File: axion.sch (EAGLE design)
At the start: 146 parts, among them IC1 3.3V, IC2 5V, Q2 12.288Mhz, U10 MIC2039, U11 WM8731, U2 Intel Edison, U4 FT232RLSSOP, U5 PCA9306D, U6 74HC4050, U7 TPA2005D1DGN, X1 MKDSN1,5/2-5,08, X2 ZX62R-AB-5P, X3 ST-005-G, X4 ZX62R-B-5P

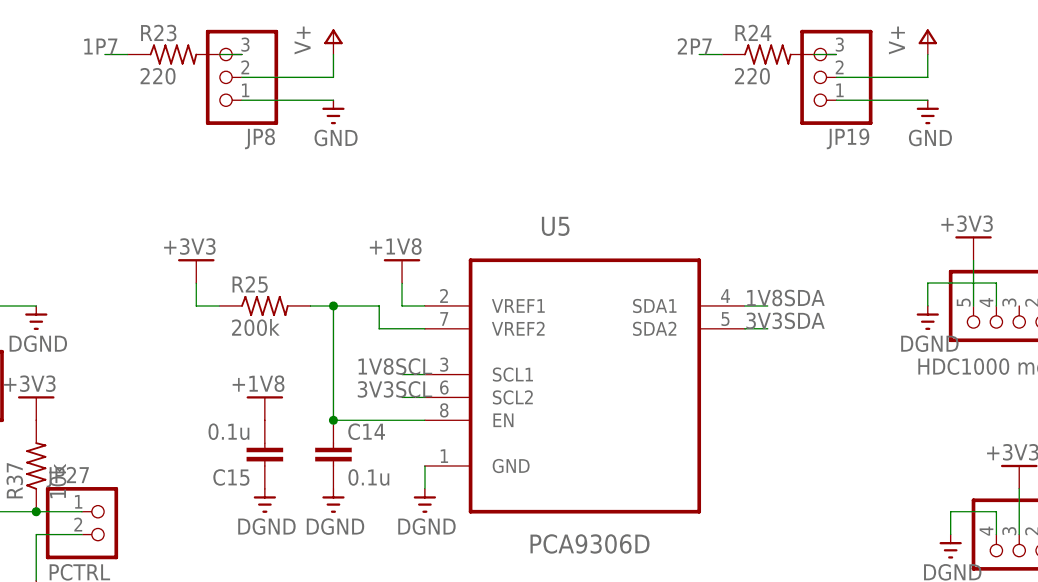
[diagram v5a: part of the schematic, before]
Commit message: Add 820 pullup to 1v8 side of I2c
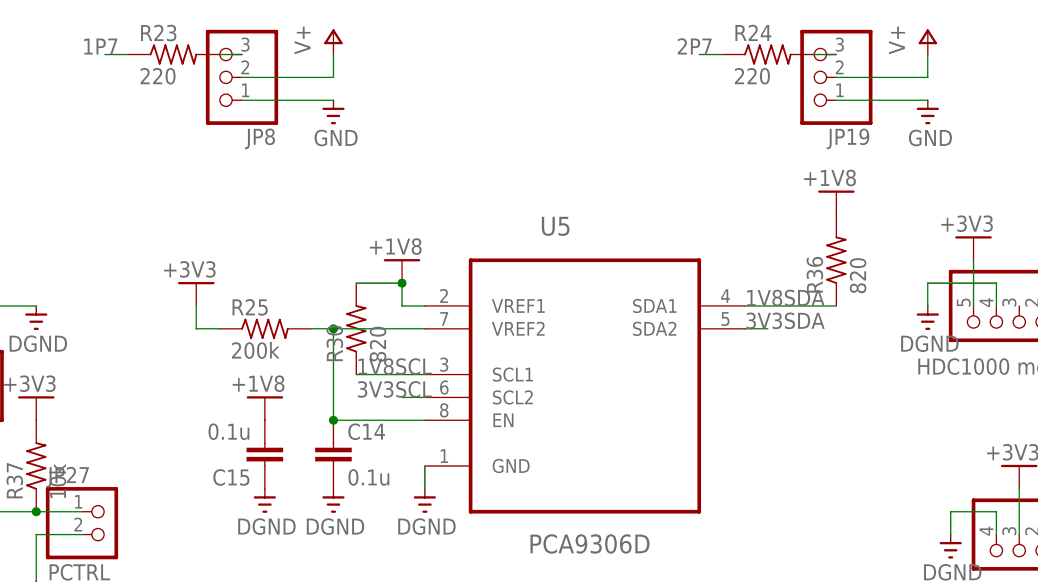
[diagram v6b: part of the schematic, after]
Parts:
- added R30, R36: 820, resistor:R-US_M1206
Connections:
- net +1V8: now also R30.2, R36.2
- net 1V8SCL: now also R30.1
- net 1V8SDA: now also R36.1
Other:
- moved on the sheet: R25
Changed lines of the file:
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@@
 <part name="DGND34" library="supply0" deviceset="DGND" device=""/>
 <part name="V43" library="supply0" deviceset="+3V3" device=""/>
+<part name="R30" library="resistor" deviceset="R-US_" device="M1206" value="820"/>
+<part name="R36" library="resistor" deviceset="R-US_" device="M1206" value="820"/>
+<part name="V25" library="supply0" deviceset="+1V8" device=""/>
 </parts>
 <sheets>
@@
 <instance part="C11" gate="G$1" x="-106.68" y="0"/>
 <instance part="DGND13" gate="G$1" x="-106.68" y="-7.62"/>
-<instance part="R25" gate="G$1" x="165.1" y="-68.58"/>
+<instance part="R25" gate="G$1" x="165.1" y="-71.12"/>
 <instance part="C14" gate="G$1" x="172.72" y="-83.82"/>
 <instance part="C15" gate="G$1" x="165.1" y="-86.36" rot="R180"/>
@@
 <instance part="JP28" gate="G$1" x="137.16" y="-127"/>
 <instance part="U9" gate="G$1" x="48.26" y="-7.62"/>
-<instance part="V27" gate="G$1" x="157.48" y="-63.5"/>
+<instance part="V27" gate="G$1" x="157.48" y="-66.04"/>
 <instance part="V2" gate="G$1" x="12.7" y="68.58"/>
 <instance part="V3" gate="G$1" x="15.24" y="91.44"/>
@@
 <instance part="DGND34" gate="G$1" x="78.74" y="-17.78"/>
 <instance part="V43" gate="G$1" x="78.74" y="-7.62"/>
+<instance part="R30" gate="G$1" x="175.26" y="-71.12" rot="R90"/>
+<instance part="R36" gate="G$1" x="228.6" y="-63.5" rot="R90"/>
+<instance part="V25" gate="G$1" x="228.6" y="-55.88"/>
 </instances>
 <busses>
@@
 </segment>
 <segment>
-<wire x1="157.48" y1="-66.04" x2="157.48" y2="-68.58" width="0.1524" layer="91"/>
+<wire x1="157.48" y1="-68.58" x2="157.48" y2="-71.12" width="0.1524" layer="91"/>
 <pinref part="R25" gate="G$1" pin="1"/>
-<wire x1="157.48" y1="-68.58" x2="160.02" y2="-68.58" width="0.1524" layer="91"/>
+<wire x1="157.48" y1="-71.12" x2="160.02" y2="-71.12" width="0.1524" layer="91"/>
 <pinref part="V27" gate="G$1" pin="+3V3"/>
 </segment>
@@
 <wire x1="182.88" y1="-68.58" x2="180.34" y2="-68.58" width="0.1524" layer="91"/>
 <wire x1="180.34" y1="-68.58" x2="180.34" y2="-66.04" width="0.1524" layer="91"/>
+<pinref part="R30" gate="G$1" pin="2"/>
+<wire x1="175.26" y1="-66.04" x2="180.34" y2="-66.04" width="0.1524" layer="91"/>
+<junction x="180.34" y="-66.04"/>
 </segment>
 <segment>
@@
 <pinref part="V35" gate="G$1" pin="+1V8"/>
 </segment>
+<segment>
+<pinref part="R36" gate="G$1" pin="2"/>
+<pinref part="V25" gate="G$1" pin="+1V8"/>
+</segment>
 </net>
 <net name="UART_TXD" class="0">
@@
 <segment>
 <pinref part="U5" gate="A" pin="SDA1"/>
-<wire x1="218.44" y1="-68.58" x2="220.98" y2="-68.58" width="0.1524" layer="91"/>
 <label x="218.44" y="-68.58" size="1.778" layer="95"/>
+<pinref part="R36" gate="G$1" pin="1"/>
+<wire x1="228.6" y1="-68.58" x2="218.44" y2="-68.58" width="0.1524" layer="91"/>
 </segment>
 <segment>
@@
 <segment>
 <pinref part="U5" gate="A" pin="SCL1"/>
-<wire x1="180.34" y1="-76.2" x2="182.88" y2="-76.2" width="0.1524" layer="91"/>
 <label x="175.26" y="-76.2" size="1.778" layer="95"/>
+<pinref part="R30" gate="G$1" pin="1"/>
+<wire x1="182.88" y1="-76.2" x2="175.26" y2="-76.2" width="0.1524" layer="91"/>
 </segment>
 <segment>
@@
 <pinref part="R25" gate="G$1" pin="2"/>
 <pinref part="U5" gate="A" pin="EN"/>
-<wire x1="172.72" y1="-68.58" x2="170.18" y2="-68.58" width="0.1524" layer="91"/>
+<wire x1="172.72" y1="-71.12" x2="170.18" y2="-71.12" width="0.1524" layer="91"/>
 <wire x1="182.88" y1="-81.28" x2="172.72" y2="-81.28" width="0.1524" layer="91"/>
-<wire x1="172.72" y1="-81.28" x2="172.72" y2="-68.58" width="0.1524" layer="91"/>
+<wire x1="172.72" y1="-81.28" x2="172.72" y2="-71.12" width="0.1524" layer="91"/>
 <pinref part="C14" gate="G$1" pin="1"/>
 <junction x="172.72" y="-81.28"/>
 <pinref part="U5" gate="A" pin="VREF2"/>
-<wire x1="182.88" y1="-71.12" x2="177.8" y2="-71.12" width="0.1524" layer="91"/>
-<wire x1="177.8" y1="-71.12" x2="177.8" y2="-68.58" width="0.1524" layer="91"/>
-<wire x1="177.8" y1="-68.58" x2="172.72" y2="-68.58" width="0.1524" layer="91"/>
-<junction x="172.72" y="-68.58"/>
-</segment>
-</net>
+<wire x1="182.88" y1="-71.12" x2="172.72" y2="-71.12" width="0.1524" layer="91"/>
+<junction x="172.72" y="-71.12"/>
+</segment>
+</net>
